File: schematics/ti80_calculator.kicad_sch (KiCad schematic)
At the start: 138 parts, among them J1 Open, J10 0, J13 0, J14 0Ω, J15 0Ω, J16 0, J17 0Ω, J18 0, J5 0Ω, J7 0Ω, J8 0, J9 0Ω, Q2 LG, Q3 LG, Q4 RIQ, SW1 Slide Switch, SW10 CLEAR, SW11 VARS, SW12 PRGM, SW13 FRAC, SW14 MATH, SW15 MODE, SW17 ^, SW18 TAN, SW19 COS, SW2 ON, SW20 SIN, SW21 x⁻¹, SW22 2nd, SW24 ÷, SW25 ), SW26 (, SW27 ,, SW28 x², SW29 Y=, SW30 ▲, SW31 ×, SW32 9, SW33 8, SW34 7, SW35 LOG, SW36 WINDOW, SW37 ►, SW38 -, SW39 6, SW40 5, SW41 4, SW42 LN, SW43 ZOOM, SW44 ◄, SW45 +, SW46 3, SW47 2, SW48 1, SW49 STO►, SW5 STAT, SW50 TRACE, SW51 ▼, SW52 ENTER, SW53 (-), SW54 •, SW55 0, SW57 GRAPH, SW6 X,T, SW7 ALPHA, SW8 DEL, U1 T6M53A, U2 LH5359, U3 SRM2264, U4 T6B79

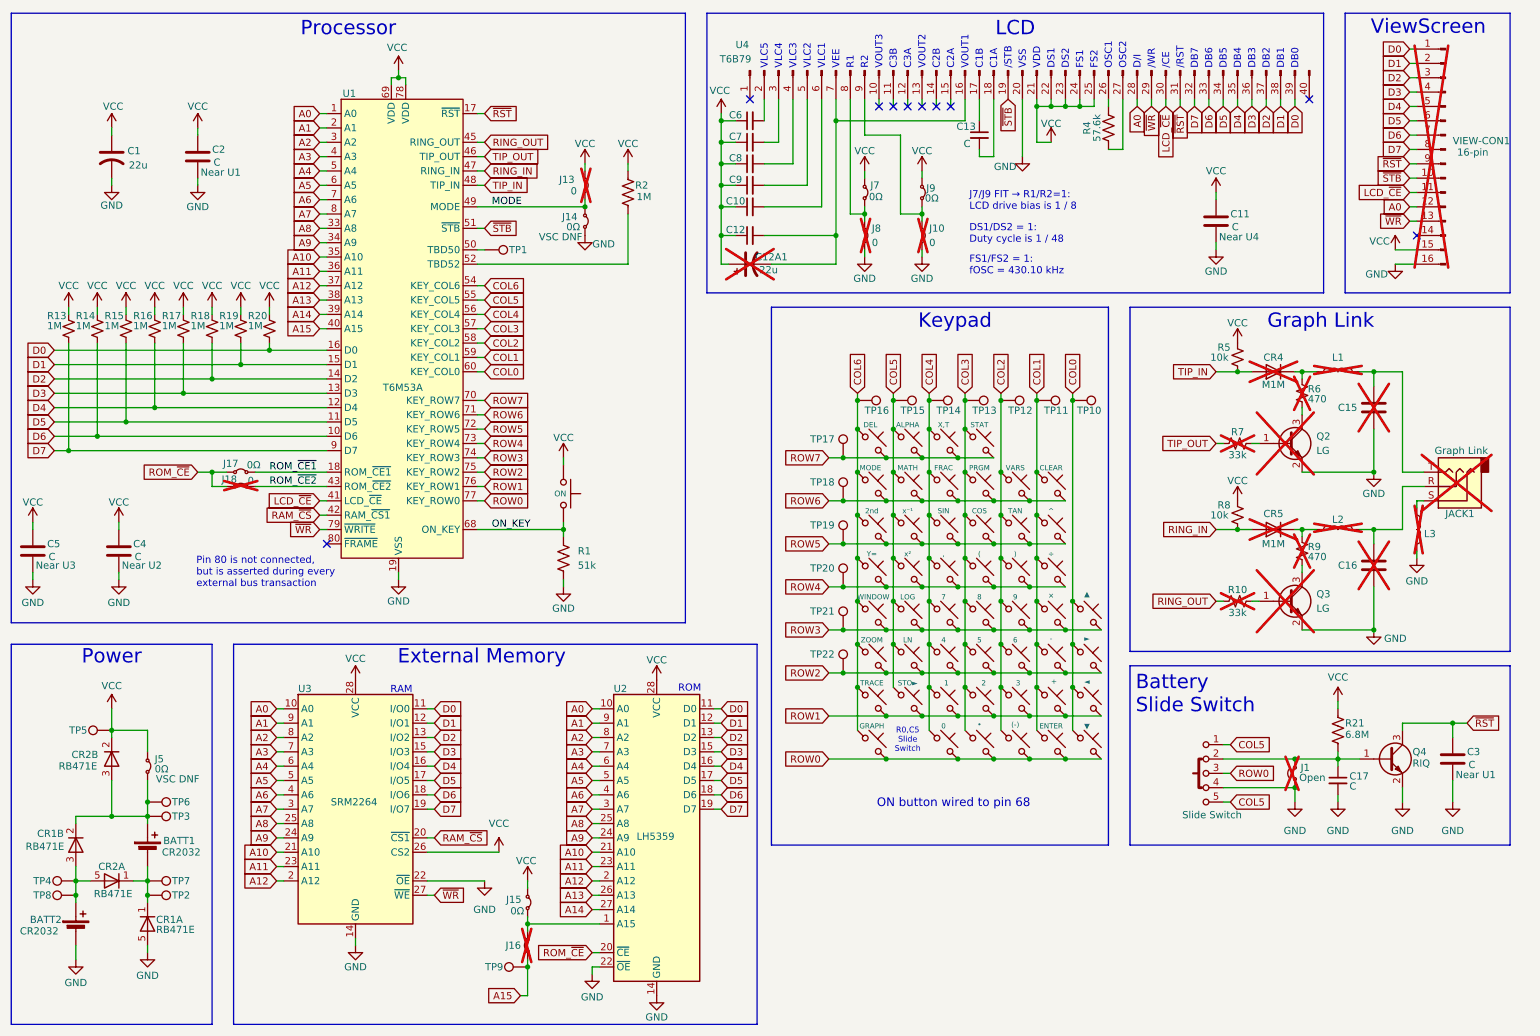
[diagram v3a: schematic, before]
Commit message: Reorganize the bypass caps and bump rev 3
- Clean up layout of the U2/U3 capacitors
- Add more to title and bump revision to 3
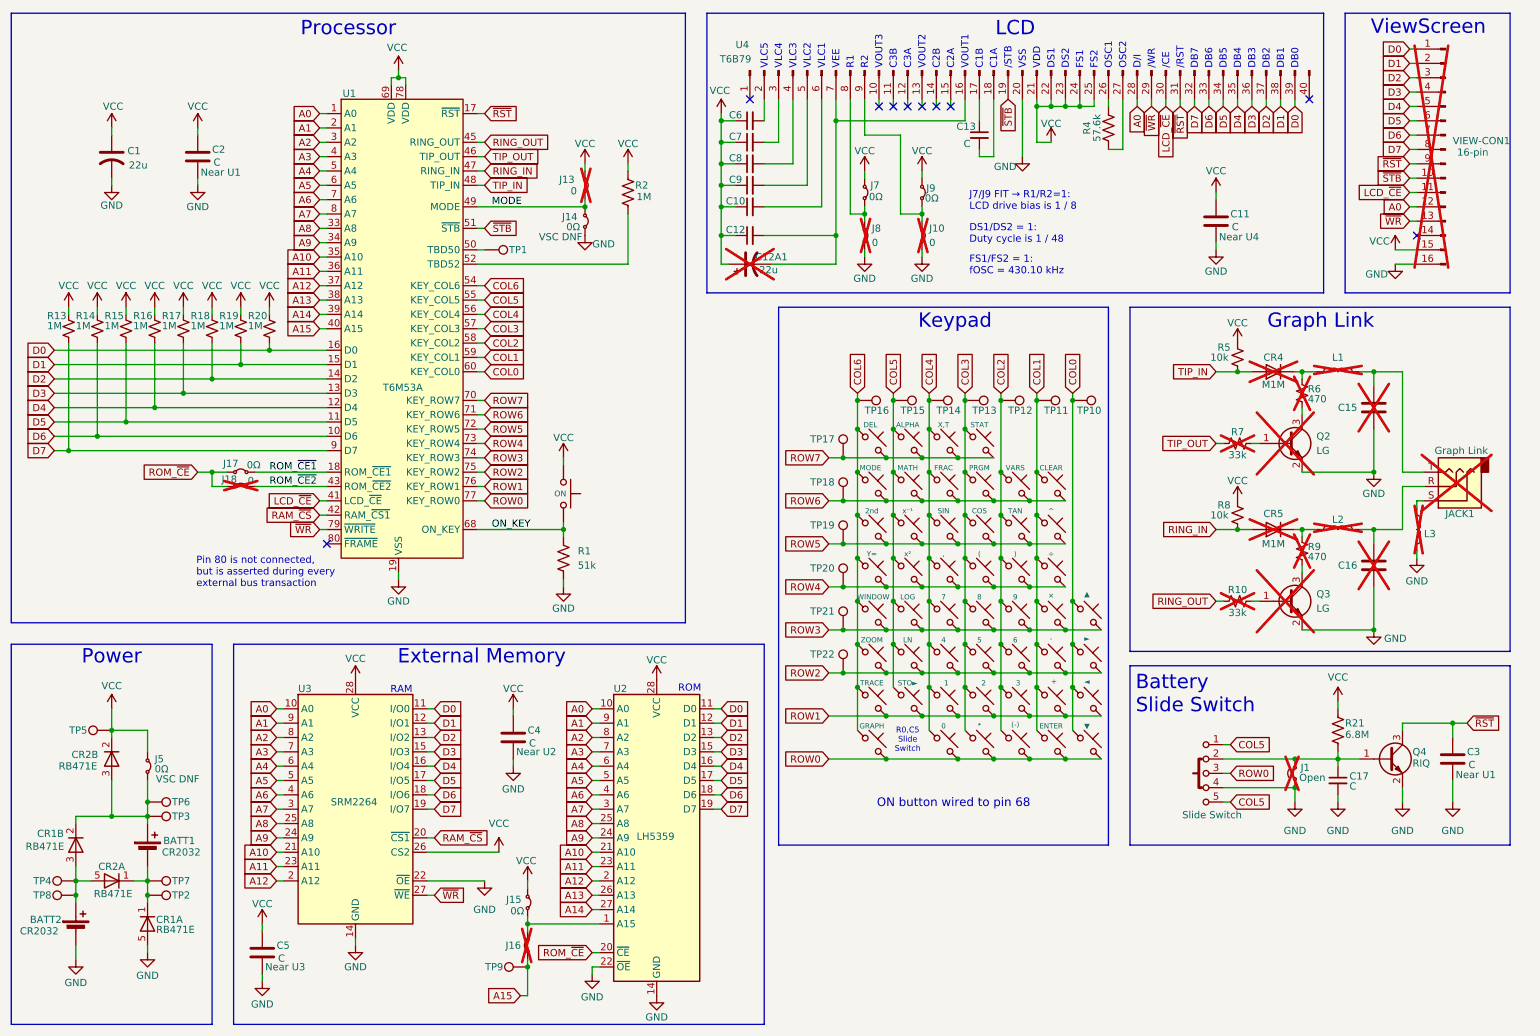
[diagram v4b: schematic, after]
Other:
- title: TI-80 Calculator -> TI-80 Graphing Calculator
- moved on the sheet: C4, C5
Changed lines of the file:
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@@
 	(paper "A4")
 	(title_block
-		(title "TI-80 Calculator")
-		(date "2025-Aug-24")
-		(rev "2")
+		(title "TI-80 Graphing Calculator")
+		(date "2025-Aug-25")
+		(rev "3")
 	)
 	(rectangle
@@
 	(rectangle
 		(start 54.61 127)
-		(end 147.32 194.31)
+		(end 148.59 194.31)
 		(stroke
 			(width 0)
@@
 	)
 	(rectangle
-		(start 149.86 67.31)
+		(start 151.13 67.31)
 		(end 209.55 162.56)
 		(stroke
@@
 	(wire
 		(pts
-			(xy 34.29 105.41) (xy 34.29 106.68)
+			(xy 104.14 138.43) (xy 104.14 139.7)
 		)
 		(stroke
@@
 	(wire
 		(pts
-			(xy 34.29 114.3) (xy 34.29 115.57)
+			(xy 104.14 147.32) (xy 104.14 148.59)
 		)
 		(stroke
@@
 	(wire
 		(pts
-			(xy 19.05 114.3) (xy 19.05 115.57)
+			(xy 59.69 185.42) (xy 59.69 186.69)
 		)
 		(stroke
@@
 	(wire
 		(pts
-			(xy 19.05 105.41) (xy 19.05 106.68)
+			(xy 59.69 176.53) (xy 59.69 177.8)
 		)
 		(stroke
@@
 	(symbol
 		(lib_id "power:VCC")
-		(at 34.29 105.41 0)
+		(at 104.14 138.43 0)
 		(unit 1)
 		(exclude_from_sim no)
@@
 		(dnp no)
 		(property "Reference" "#PWR030"
-			(at 34.29 109.22 0)
+			(at 104.14 142.24 0)
 			(effects
 				(font
@@
 		)
 		(property "Value" "VCC"
-			(at 34.29 101.854 0)
+			(at 104.14 134.874 0)
 			(effects
 				(font
@@
 		)
 		(property "Footprint" ""
-			(at 34.29 105.41 0)
+			(at 104.14 138.43 0)
 			(effects
 				(font
@@
 		)
 		(property "Datasheet" ""
-			(at 34.29 105.41 0)
+			(at 104.14 138.43 0)
 			(effects
 				(font
@@
 		)
 		(property "Description" "Power symbol creates a global label with name \"VCC\""
-			(at 34.29 105.41 0)
+			(at 104.14 138.43 0)
 			(effects
 				(font
@@
 	(symbol
 		(lib_id "Device:C")
-		(at 19.05 110.49 0)
+		(at 59.69 181.61 0)
 		(unit 1)
 		(exclude_from_sim no)
@@
 		(dnp no)
 		(property "Reference" "C5"
-			(at 21.59 109.22 0)
+			(at 62.23 180.34 0)
 			(effects
 				(font
@@
 		)
 		(property "Value" "C"
-			(at 21.844 111.506 0)
+			(at 62.484 182.626 0)
 			(effects
 				(font
@@
 		)
 		(property "Footprint" "Capacitor_SMD:C_0805_2012Metric"
-			(at 20.0152 114.3 0)
+			(at 60.6552 185.42 0)
 			(effects
 				(font
@@
 		)
 		(property "Datasheet" "~"
-			(at 19.05 110.49 0)
+			(at 59.69 181.61 0)
 			(effects
 				(font
@@
 		)
 		(property "Description" "Unpolarized capacitor"
-			(at 19.05 110.49 0)
+			(at 59.69 181.61 0)
 			(effects
 				(font
@@
 		)
 		(property "Placement" "Near U3"
-			(at 23.114 113.03 0)
+			(at 63.754 184.15 0)
 			(effects
 				(font
@@
 	(symbol
 		(lib_id "power:GND")
-		(at 34.29 115.57 0)
+		(at 104.14 148.59 0)
 		(unit 1)
 		(exclude_from_sim no)
@@
 		(dnp no)
 		(property "Reference" "#PWR032"
-			(at 34.29 121.92 0)
+			(at 104.14 154.94 0)
 			(effects
 				(font
@@
 		)
 		(property "Value" "GND"
-			(at 34.29 119.634 0)
+			(at 104.14 152.654 0)
 			(effects
 				(font
@@
 		)
 		(property "Footprint" ""
-			(at 34.29 115.57 0)
+			(at 104.14 148.59 0)
 			(effects
 				(font
@@
 		)
 		(property "Datasheet" ""
-			(at 34.29 115.57 0)
+			(at 104.14 148.59 0)
 			(effects
 				(font
@@
 		)
 		(property "Description" "Power symbol creates a global label with name \"GND\" , ground"
-			(at 34.29 115.57 0)
+			(at 104.14 148.59 0)
 			(effects
 				(font
@@
 	(symbol
 		(lib_id "Device:C")
-		(at 34.29 110.49 0)
+		(at 104.14 143.51 0)
 		(unit 1)
 		(exclude_from_sim no)
@@
 		(dnp no)
 		(property "Reference" "C4"
-			(at 36.83 109.22 0)
+			(at 106.68 142.24 0)
 			(effects
 				(font
@@
 		)
 		(property "Value" "C"
-			(at 37.084 111.506 0)
+			(at 106.934 144.526 0)
 			(effects
 				(font
@@
 		)
 		(property "Footprint" "Capacitor_SMD:C_0805_2012Metric"
-			(at 35.2552 114.3 0)
+			(at 105.1052 147.32 0)
 			(effects
 				(font
@@
 		)
 		(property "Datasheet" "~"
-			(at 34.29 110.49 0)
+			(at 104.14 143.51 0)
 			(effects
 				(font
@@
 		)
 		(property "Description" "Unpolarized capacitor"
-			(at 34.29 110.49 0)
+			(at 104.14 143.51 0)
 			(effects
 				(font
@@
 		)
 		(property "Placement" "Near U2"
-			(at 38.354 113.03 0)
+			(at 108.204 146.05 0)
 			(effects
 				(font
@@
 	(symbol
 		(lib_id "power:VCC")
-		(at 19.05 105.41 0)
+		(at 59.69 176.53 0)
 		(unit 1)
 		(exclude_from_sim no)
@@
 		(dnp no)
 		(property "Reference" "#PWR027"
-			(at 19.05 109.22 0)
+			(at 59.69 180.34 0)
 			(effects
 				(font
@@
 		)
 		(property "Value" "VCC"
-			(at 19.05 101.854 0)
+			(at 59.69 172.974 0)
 			(effects
 				(font
@@
 		)
 		(property "Footprint" ""
-			(at 19.05 105.41 0)
+			(at 59.69 176.53 0)
 			(effects
 				(font
@@
 		)
 		(property "Datasheet" ""
-			(at 19.05 105.41 0)
+			(at 59.69 176.53 0)
 			(effects
 				(font
@@
 		)
 		(property "Description" "Power symbol creates a global label with name \"VCC\""
-			(at 19.05 105.41 0)
+			(at 59.69 176.53 0)
 			(effects
 				(font
@@
 	(symbol
 		(lib_id "power:GND")
-		(at 19.05 115.57 0)
+		(at 59.69 186.69 0)
 		(unit 1)
 		(exclude_from_sim no)
@@
 		(dnp no)
 		(property "Reference" "#PWR026"
-			(at 19.05 121.92 0)
+			(at 59.69 193.04 0)
 			(effects
 				(font
@@
 		)
 		(property "Value" "GND"
-			(at 19.05 119.634 0)
+			(at 59.69 190.754 0)
 			(effects
 				(font
@@
 		)
 		(property "Footprint" ""
-			(at 19.05 115.57 0)
+			(at 59.69 186.69 0)
 			(effects
 				(font
@@
 		)
 		(property "Datasheet" ""
-			(at 19.05 115.57 0)
+			(at 59.69 186.69 0)
 			(effects
 				(font
@@
 		)
 		(property "Description" "Power symbol creates a global label with name \"GND\" , ground"
-			(at 19.05 115.57 0)
+			(at 59.69 186.69 0)
 			(effects
 				(font

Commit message: Change inductor package from 1210 to 1008 and hide test point silkscreens
- 1008 is likely better package size for unpopulated graph link inductors
- Remove the test point "TP" silkscreen labels
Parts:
- L1, L2, L3: footprint Inductor_SMD:L_1210_3225Metric -> Inductor_SMD:L_1008_2520Metric_Pad1.43x2.20mm_HandSolder
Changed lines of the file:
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@@
 			)
 		)
-		(property "Footprint" "Inductor_SMD:L_1210_3225Metric"
+		(property "Footprint" "Inductor_SMD:L_1008_2520Metric_Pad1.43x2.20mm_HandSolder"
 			(at 264.16 106.68 0)
 			(effects
@@
 			)
 		)
-		(property "Footprint" "Inductor_SMD:L_1210_3225Metric"
+		(property "Footprint" "Inductor_SMD:L_1008_2520Metric_Pad1.43x2.20mm_HandSolder"
 			(at 250.19 106.68 0)
 			(effects
@@
 			)
 		)
-		(property "Footprint" "Inductor_SMD:L_1210_3225Metric"
+		(property "Footprint" "Inductor_SMD:L_1008_2520Metric_Pad1.43x2.20mm_HandSolder"
 			(at 250.19 78.74 0)
 			(effects
